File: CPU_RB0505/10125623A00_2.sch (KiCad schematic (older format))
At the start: 30 parts, among them IC1 TL16C750IPM, IC13 K9F1G08UOA-PCB0, IC14 74ACT16373, IC2 SN74ALVC164245, IC32 25LC320, IC38 74HCT1G08GW, IC39 74HCT04GW, IC5 74HCT1G32GW, IC7 29F400-70EC, IC8 SN74LVC1G07DBVT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

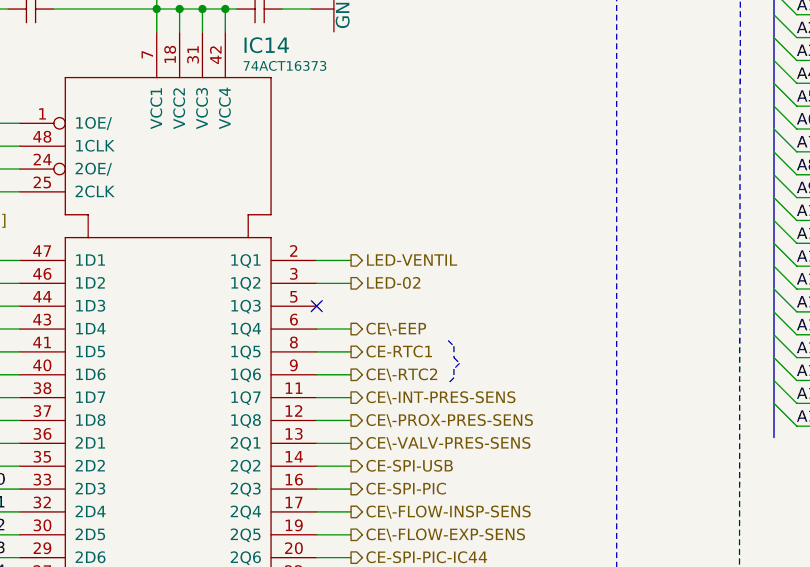
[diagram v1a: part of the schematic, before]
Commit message: Zero/Oh confusion: LED-02 => LED-O2, MRST-SPI-O_E => MRST-SPI-0_E
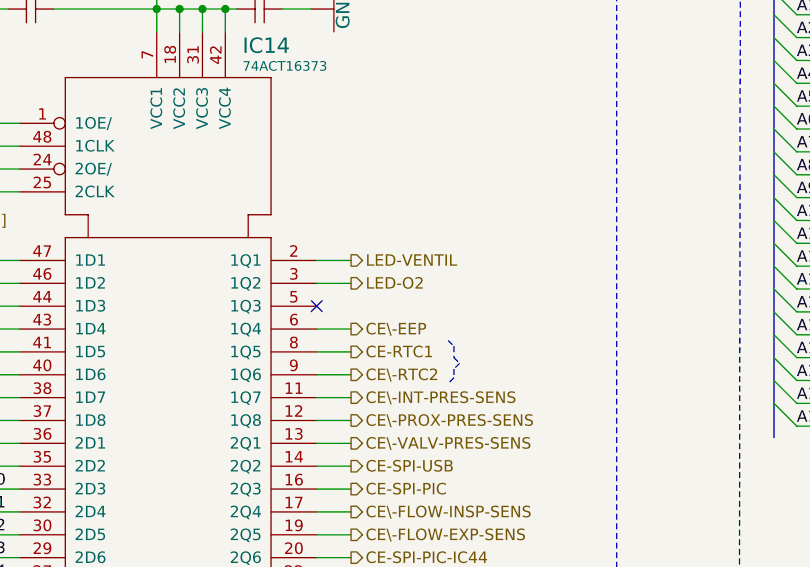
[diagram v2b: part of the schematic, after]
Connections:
- net LED-02 renamed LED-O2
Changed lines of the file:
@@
 LED-VENTIL
 Text HLabel 5625 2900 2    50   Output ~ 0
-LED-02
+LED-O2
 Text HLabel 5625 3100 2    50   Output ~ 0
 CE\-EEP

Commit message: back anotate from cmp file
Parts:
- C140, C15, C2, C24, C30, C33, C37, C4: footprint 10125623A00:C0805 -> AllModules:C0402_1
- C16: footprint 10125623A00:C0805 -> AllModules:C0603_1
- C20, C5: footprint 10125623A00:C0603 -> AllModules:C0402_1
- IC1: footprint 10125623A00:TQFP64 -> AllModules:TQFP64_1
- IC13, IC7: footprint 10125623A00:TS048 -> AllModules:TSOP48-ENT9.965_1
- IC14: footprint 10125623A00:TSSOP48 -> AllModules:SSOP48_1
- IC2: footprint 10125623A00:TSSOP48 -> AllModules:TSSOP48_1
- IC32: footprint 10125623A00:SOIC8 -> AllModules:MX.A8_COMPOSANT_1
- IC38, IC39, IC5: footprint 10125623A00:SOT23-5 -> AllModules:SC70-5_1
- IC8, IC9: footprint 10125623A00:SOT753_DBV -> AllModules:SOT23-5_1
- JP5, JP6: footprint 10125623A00:0805 -> AllModules:R0603_1
- Q2: footprint 10125623A00:HC49UP -> AllModules:HC49-4HSMX_1
- R2, R4, R5, R6: footprint 10125623A00:R0805 -> AllModules:R0603_1
- RS8: footprint 10125623A00:BCN16_4_ -> AllModules:BCN16_1
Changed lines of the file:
@@
 F 0 "C33" V 4450 1594 64  0000 L BNN
 F 1 "100nF" V 4356 1601 42  0000 L BNN
-F 2 "10125623A00:C0805" H 4225 1700 50  0001 C CNN
+F 2 "AllModules:C0402_1" H 4225 1700 50  0001 C CNN
 F 3 "" H 4225 1700 50  0001 C CNN
 F 4 "CAPACITOR,100NF,16V,+/-10%,X7R,0402" H 4225 1700 50  0001 C CNN "Description"
@@
 F 0 "C37" V 5450 1607 64  0000 L BNN
 F 1 "100nF" V 5356 1601 42  0000 L BNN
-F 2 "10125623A00:C0805" H 5225 1700 50  0001 C CNN
+F 2 "AllModules:C0402_1" H 5225 1700 50  0001 C CNN
 F 3 "" H 5225 1700 50  0001 C CNN
 F 4 "CAPACITOR,100NF,16V,+/-10%,X7R,0402" H 5225 1700 50  0001 C CNN "Description"
@@
 F 0 "C2" V 12487 1394 64  0000 R TNN
 F 1 "100nF" V 12418 1387 42  0000 R TNN
-F 2 "10125623A00:C0805" H 12325 1325 50  0001 C CNN
+F 2 "AllModules:C0402_1" H 12325 1325 50  0001 C CNN
 F 3 "" H 12325 1325 50  0001 C CNN
 F 4 "CAPACITOR,100NF,16V,+/-10%,X7R,0402" H 12325 1325 50  0001 C CNN "Description"
@@
 F 0 "Q2" V 13690 1950 64  0000 R TNN
 F 1 "3.6864MHz" V 13775 2188 42  0000 R TNN
-F 2 "10125623A00:HC49UP" H 13775 1750 50  0001 C CNN
+F 2 "AllModules:HC49-4HSMX_1" H 13775 1750 50  0001 C CNN
 F 3 "" H 13775 1750 50  0001 C CNN
 F 4 "CRYSTAL, QUARTZ, 3.6864MHZ" H 13775 1750 50  0001 C CNN "Description"
@@
 F 0 "C15" V 14162 2043 64  0000 R TNN
 F 1 "47pF" V 14256 2037 42  0000 R TNN
-F 2 "10125623A00:C0805" H 14075 1950 50  0001 C CNN
+F 2 "AllModules:C0402_1" H 14075 1950 50  0001 C CNN
 F 3 "" H 14075 1950 50  0001 C CNN
 F 4 "CAPACITOR,47 PF,+/-5%,50V,0402" H 14075 1950 50  0001 C CNN "Description"
@@
 F 0 "C16" V 14450 1432 64  0000 L BNN
 F 1 "22pF" V 14356 1438 42  0000 L BNN
-F 2 "10125623A00:C0805" H 14200 1525 50  0001 C CNN
+F 2 "AllModules:C0603_1" H 14200 1525 50  0001 C CNN
 F 3 "" H 14200 1525 50  0001 C CNN
 F 4 "CAPACITOR CERAMIC,22PF,+/-5%,50V,0603" H 14200 1525 50  0001 C CNN "Description"
@@
 F 0 "R2" H 13225 1800 64  0000 L BNN
 F 1 "1.5k" H 13225 1738 42  0000 L BNN
-F 2 "10125623A00:R0805" H 13300 1950 50  0001 C CNN
+F 2 "AllModules:R0603_1" H 13300 1950 50  0001 C CNN
 F 3 "" H 13300 1950 50  0001 C CNN
 F 4 "RESISTOR 1.5K OHM, 0603, +/-5%" H 13300 1950 50  0001 C CNN "Description"
@@
 F 0 "IC1" H 12650 4625 59  0000 L BNN
 F 1 "TL16C750IPM" H 12650 4538 42  0000 L BNN
-F 2 "10125623A00:TQFP64" H 12200 3000 50  0001 C CNN
+F 2 "AllModules:TQFP64_1" H 12200 3000 50  0001 C CNN
 F 3 "" H 12200 3000 50  0001 C CNN
 F 4 "UART, LQFP64" H 12200 3000 50  0001 C CNN "Description"
@@
 F 0 "RS8" V 13425 3425 59  0000 L BNN
 F 1 "6.8k" V 13338 3425 59  0000 L BNN
-F 2 "10125623A00:BCN16_4_" H 13350 3200 50  0001 C CNN
+F 2 "AllModules:BCN16_1" H 13350 3200 50  0001 C CNN
 F 3 "" H 13350 3200 50  0001 C CNN
 F 4 "RESISTOR ARRAY, 6.8K OHM, +/-5%, 1206" H 13350 3200 50  0001 C CNN "Description"
@@
 F 0 "IC8" H 14600 7112 64  0000 L BNN
 F 1 "SN74LVC1G07DBVT" H 14575 7025 42  0000 L BNN
-F 2 "10125623A00:SOT753_DBV" H 14250 6650 50  0001 C CNN
+F 2 "AllModules:SOT23-5_1" H 14250 6650 50  0001 C CNN
 F 3 "" H 14250 6650 50  0001 C CNN
 F 4 "BUFFER WITH OPEN DRAIN OUTPUT,SOT23" H 14250 6650 50  0001 C CNN "Description"
@@
 F 0 "R5" V 13613 3925 64  0000 R TNN
 F 1 "10k" V 13550 3925 42  0000 R TNN
-F 2 "10125623A00:R0805" H 13600 4000 50  0001 C CNN
+F 2 "AllModules:R0603_1" H 13600 4000 50  0001 C CNN
 F 3 "" H 13600 4000 50  0001 C CNN
 F 4 "RESISTOR,10K OHM, 0.063W,+/-5%,0603" H 13600 4000 50  0001 C CNN "Description"
@@
 F 0 "R6" V 15300 6200 64  0000 R TNN
 F 1 "10k" V 15225 6200 42  0000 R TNN
-F 2 "10125623A00:R0805" H 15275 6350 50  0001 C CNN
+F 2 "AllModules:R0603_1" H 15275 6350 50  0001 C CNN
 F 3 "" H 15275 6350 50  0001 C CNN
 F 4 "RESISTOR,10K OHM, 0.063W,+/-5%,0603" H 15275 6350 50  0001 C CNN "Description"
@@
 F 0 "C140" V 3000 1606 64  0000 L BNN
 F 1 "100nF" V 3069 1625 42  0000 L BNN
-F 2 "10125623A00:C0805" H 3150 1725 50  0001 C CNN
+F 2 "AllModules:C0402_1" H 3150 1725 50  0001 C CNN
 F 3 "" H 3150 1725 50  0001 C CNN
 	1    3150 1725
@@
 F 0 "C4" V 7125 6719 64  0000 L BNN
 F 1 "100nF" V 7031 6676 42  0000 L BNN
-F 2 "10125623A00:C0805" H 6900 6800 50  0001 C CNN
+F 2 "AllModules:C0402_1" H 6900 6800 50  0001 C CNN
 F 3 "" H 6900 6800 50  0001 C CNN
 F 4 "CAPACITOR,100NF,16V,+/-10%,X7R,0402" H 6900 6800 50  0001 C CNN "Description"
@@
 F 0 "C24" V 10887 6819 64  0000 R TNN
 F 1 "100nF" V 10818 6813 42  0000 R TNN
-F 2 "10125623A00:C0805" H 10725 6725 50  0001 C CNN
+F 2 "AllModules:C0402_1" H 10725 6725 50  0001 C CNN
 F 3 "" H 10725 6725 50  0001 C CNN
 F 4 "CAPACITOR,100NF,16V,+/-10%,X7R,0402" H 10725 6725 50  0001 C CNN "Description"
@@
 F 0 "C5" V 3825 6857 64  0000 L BNN
 F 1 "100nF" V 3731 6788 42  0000 L BNN
-F 2 "10125623A00:C0603" H 3600 6900 50  0001 C CNN
+F 2 "AllModules:C0402_1" H 3600 6900 50  0001 C CNN
 F 3 "" H 3600 6900 50  0001 C CNN
 F 4 "CAPACITOR,100NF,16V,+/-10%,X7R,0402" H 3600 6900 50  0001 C CNN "Description"
@@
 F 0 "C20" V 4800 6844 64  0000 L BNN
 F 1 "100nF" V 4706 6826 42  0000 L BNN
-F 2 "10125623A00:C0603" H 4575 6900 50  0001 C CNN
+F 2 "AllModules:C0402_1" H 4575 6900 50  0001 C CNN
 F 3 "" H 4575 6900 50  0001 C CNN
 F 4 "CAPACITOR,100NF,16V,+/-10%,X7R,0402" H 4575 6900 50  0001 C CNN "Description"
@@
 F 0 "JP6" H 14475 5525 51  0000 L BNN
 F 1 "JUMP_0U" H 14000 5525 51  0001 L BNN
-F 2 "10125623A00:0805" H 14550 5450 50  0001 C CNN
+F 2 "AllModules:R0603_1" H 14550 5450 50  0001 C CNN
 F 3 "" H 14550 5450 50  0001 C CNN
 F 4 "RESISTANCE, 0 OHM,0603" H 14550 5450 50  0001 C CNN "Description"
@@
 F 0 "IC13" H 7350 8625 64  0000 L BNN
 F 1 "K9F1G08UOA-PCB0" H 7350 8537 42  0000 L BNN
-F 2 "10125623A00:TS048" H 6400 7900 50  0001 C CNN
+F 2 "AllModules:TSOP48-ENT9.965_1" H 6400 7900 50  0001 C CNN
 F 3 "" H 6400 7900 50  0001 C CNN
 F 4 "MEMORY NAND FLASH, 1G, 2.7 TO 3.6V, BUS X 8,TSOP" H 6400 7900 50  0001 C CNN "Description"
@@
 F 0 "IC39" H 2238 2925 67  0000 L BNN
 F 1 "74HCT04GW" H 2238 2850 42  0000 L BNN
-F 2 "10125623A00:SOT23-5" H 1650 2175 50  0001 C CNN
+F 2 "AllModules:SC70-5_1" H 1650 2175 50  0001 C CNN
 F 3 "" H 1650 2175 50  0001 C CNN
 F 4 "IC, INVERTER,SOT353" H 1650 2175 50  0001 C CNN "Description"
@@
 F 0 "C30" V 8763 1356 64  0000 R TNN
 F 1 "100nF" V 8694 1350 42  0000 R TNN
-F 2 "10125623A00:C0805" H 8600 1300 50  0001 C CNN
+F 2 "AllModules:C0402_1" H 8600 1300 50  0001 C CNN
 F 3 "" H 8600 1300 50  0001 C CNN
 F 4 "CAPACITOR,100NF,16V,+/-10%,X7R,0402" H 8600 1300 50  0001 C CNN "Description"
@@
 F 0 "IC7" H 8975 4725 64  0000 L BNN
 F 1 "29F400-70EC" H 8975 4650 42  0000 L BNN
-F 2 "10125623A00:TS048" H 8575 3125 50  0001 C CNN
+F 2 "AllModules:TSOP48-ENT9.965_1" H 8575 3125 50  0001 C CNN
 F 3 "" H 8575 3125 50  0001 C CNN
 F 4 "IC, FLASH MEMORY,TSOP48" H 8575 3125 50  0001 C CNN "Description"
@@
 F 0 "IC38" H 3350 3425 67  0000 L BNN
 F 1 "74HCT1G08GW" H 3337 3350 42  0000 L BNN
-F 2 "10125623A00:SOT23-5" H 2800 2675 50  0001 C CNN
+F 2 "AllModules:SC70-5_1" H 2800 2675 50  0001 C CNN
 F 3 "" H 2800 2675 50  0001 C CNN
 F 4 "2 INPUT AND-GATE,SOT353" H 2800 2675 50  0001 C CNN "Description"
@@
 F 0 "IC14" H 5150 4900 67  0000 L BNN
 F 1 "74ACT16373" H 5150 4825 42  0000 L BNN
-F 2 "10125623A00:TSSOP48" H 4875 3400 50  0001 C CNN
+F 2 "AllModules:SSOP48_1" H 4875 3400 50  0001 C CNN
 F 3 "" H 4875 3400 50  0001 C CNN
 F 4 "IC,16 BIT D TYPE 3STATE OP, LATCHES,SSOP" H 4875 3400 50  0001 C CNN "Description"
@@
 F 0 "IC9" H 14275 3775 64  0000 L BNN
 F 1 "SN74LVC1G07DBVT" H 13825 3875 42  0000 L BNN
-F 2 "10125623A00:SOT753_DBV" H 14400 4250 50  0001 C CNN
+F 2 "AllModules:SOT23-5_1" H 14400 4250 50  0001 C CNN
 F 3 "" H 14400 4250 50  0001 C CNN
 F 4 "BUFFER WITH OPEN DRAIN OUTPUT,SOT23" H 14400 4250 50  0001 C CNN "Description"
@@
 F 0 "JP5" H 14225 5525 51  0000 L BNN
 F 1 "JUMP_0U" H 13875 5800 51  0001 L BNN
-F 2 "10125623A00:0805" H 14300 5450 50  0001 C CNN
+F 2 "AllModules:R0603_1" H 14300 5450 50  0001 C CNN
 F 3 "" H 14300 5450 50  0001 C CNN
 	1    14300 5450
@@
 F 0 "R4" V 13625 1838 64  0000 L BNN
 F 1 "1M" V 13538 1875 42  0000 L BNN
-F 2 "10125623A00:R0805" H 13550 1750 50  0001 C CNN
+F 2 "AllModules:R0603_1" H 13550 1750 50  0001 C CNN
 F 3 "" H 13550 1750 50  0001 C CNN
 F 4 "RESISTOR,1M OHM,0.063W,+/-1%,0603" H 13550 1750 50  0001 C CNN "Description"
@@
 F 0 "IC2" H 5100 8275 67  0000 R TNN
 F 1 "SN74ALVC164245" H 5500 8175 42  0000 R TNN
-F 2 "10125623A00:TSSOP48" H 3225 7700 50  0001 C CNN
+F 2 "AllModules:TSSOP48_1" H 3225 7700 50  0001 C CNN
 F 3 "" H 3225 7700 50  0001 C CNN
 F 4 "TRANSCEIVER, 3.3V TO 5V,TSSOP" H 3225 7700 50  0001 C CNN "Description"
@@
 F 0 "IC5" H 2250 9113 64  0000 L BNN
 F 1 "74HCT1G32GW" H 2250 9038 42  0000 L BNN
-F 2 "10125623A00:SOT23-5" H 1700 8350 50  0001 C CNN
+F 2 "AllModules:SC70-5_1" H 1700 8350 50  0001 C CNN
 F 3 "" H 1700 8350 50  0001 C CNN
 F 4 "IC, 2 INPUT OR-GATE,SOT353" H 1700 8350 50  0001 C CNN "Description"
@@
 F 0 "IC32" H 10987 8287 67  0000 L BNN
 F 1 "25LC320" H 10987 8212 42  0000 L BNN
-F 2 "10125623A00:SOIC8" H 10325 7575 50  0001 C CNN
+F 2 "AllModules:MX.A8_COMPOSANT_1" H 10325 7575 50  0001 C CNN
 F 3 "" H 10325 7575 50  0001 C CNN
 F 4 "EEPROM, SOIC8" H 10325 7575 50  0001 C CNN "Description"

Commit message: fix erc errors, change many pin electrical types
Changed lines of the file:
@@
 $Descr User 17335 11946
 encoding utf-8
-Sheet 6 8
+Sheet 5 8
 Title "RB0505 CPU Board"
 Date "2020-04-15"
@@
 Wire Bus Line
 	7475 1525 7475 3575
+$Comp
+L power:PWR_FLAG #FLG0109
+U 1 1 6003889E
+P 14100 5650
+F 0 "#FLG0109" H 14100 5725 50  0001 C CNN
+F 1 "PWR_FLAG" V 14100 5777 50  0000 L CNN
+F 2 "" H 14100 5650 50  0001 C CNN
+F 3 "~" H 14100 5650 50  0001 C CNN
+	1    14100 5650
+	0    -1   -1   0
+$EndComp
+Connection ~ 14100 5650
 $EndSCHEMATC

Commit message: CPU schematic updated to Kicad resistor and cap symbols
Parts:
- C140, C15, C16, C2, C24, C30, C33, C37, C4: symbol cpu-board:C0805 -> Flipped_Devices:C_Small
- C20, C5: symbol cpu-board:C0603 -> Flipped_Devices:C_Small
- R2, R4, R5, R6: symbol cpu-board:R0805 -> Flipped_Devices:R
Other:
- moved on the sheet: C140, C16, C2, C20, C24, C30, C33, C37, C5, IC14, IC2, IC32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

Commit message: CPU board diode and transistor symbols changed to Kicad symbols
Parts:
- Q2: symbol cpu-board:HC49UP -> Device:Crystal_Small
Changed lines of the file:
@@
 $EndComp
 $Comp
-L cpu-board:HC49UP Q2
+L Device:Crystal_Small Q2
 U 1 1 53ABB1EB
 P 13800 1750

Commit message: ran renameSchSyms.py
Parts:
- C140, C2, C20, C24, C30, C33, C37, C4, C5: symbol Flipped_Devices:C_Small -> Capacitor:C0402_100nF_16V_10%
- C15: symbol Flipped_Devices:C_Small -> Capacitor:C0402_47pF_50V_5%
- C16: symbol Flipped_Devices:C_Small -> Capacitor:C0603_22pF_50V_5%
- IC1: symbol cpu-board:TL16C750IPM -> IC:TL16C750IPM
- IC13: symbol cpu-board:K9F4G08U0M-PCB000 -> IC:K9F4G08U0M-PCB000
- IC14: symbol cpu-board:74ACT16373 -> IC:74ACT16373
- IC2: symbol cpu-board:SN74ALVC164245 -> IC:SN74ALVC164245
- IC32: symbol cpu-board:AT25--- -> IC:AT25---
- IC38: symbol cpu-board:74HCT1G08GW -> IC:74HCT1G08GW
- IC39: symbol cpu-board:74HCT1G04GW -> IC:74HCT1G04GW
- IC5: symbol cpu-board:74HCT1G32GW -> IC:74HCT1G32GW
- IC7: symbol cpu-board:29F800 -> IC:29F800
- IC8, IC9: symbol cpu-board:LVC1G07DBVT -> IC:LVC1G07DBVT
- JP6: symbol cpu-board:JUMP_0U -> Jumper:JUMP_0U
- Q2: symbol Device:Crystal_Small -> Crystal:Crystal_Small_10023291
- R2: symbol Flipped_Devices:R -> Resistor:R0603_1k5_5%
- R4: symbol Flipped_Devices:R -> Resistor:R0603_1M_1%
- R5, R6: symbol Flipped_Devices:R -> Resistor:R0603_10k_5%
- RS8: symbol cpu-board:RES_4R_BCN -> Resistor:R1206_6k8_5%
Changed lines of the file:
@@
 $EndComp
 $Comp
-L Flipped_Devices:C_Small C33
+L Capacitor:C0402_100nF_16V_10% C33
 U 1 1 C9502F30
 P 4250 1700
@@
 $EndComp
 $Comp
-L Flipped_Devices:C_Small C37
+L Capacitor:C0402_100nF_16V_10% C37
 U 1 1 235E1F38
 P 5250 1700
@@
 $EndComp
 $Comp
-L Flipped_Devices:C_Small C2
+L Capacitor:C0402_100nF_16V_10% C2
 U 1 1 6D294609
 P 12300 1300
@@
 $EndComp
 $Comp
-L Device:Crystal_Small Q2
+L Crystal:Crystal_Small_10023291 Q2
 U 1 1 53ABB1EB
 P 13800 1750
@@
 $EndComp
 $Comp
-L Flipped_Devices:C_Small C15
+L Capacitor:C0402_47pF_50V_5% C15
 U 1 1 58269073
 P 14075 1950
@@
 $EndComp
 $Comp
-L Flipped_Devices:R R2
+L Resistor:R0603_1k5_5% R2
 U 1 1 986554BD
 P 13300 1950
@@
 $EndComp
 $Comp
-L cpu-board:TL16C750IPM IC1
+L IC:TL16C750IPM IC1
 U 1 1 22F7723E
 P 12200 3000
@@
 $EndComp
 $Comp
-L cpu-board:RES_4R_BCN RS8
+L Resistor:R1206_6k8_5% RS8
 U 1 1 887C726F
 P 13350 3200
@@
 $EndComp
 $Comp
-L cpu-board:LVC1G07DBVT IC8
+L IC:LVC1G07DBVT IC8
 U 1 1 45D38355
 P 14250 6650
@@
 $EndComp
 $Comp
-L Flipped_Devices:R R5
+L Resistor:R0603_10k_5% R5
 U 1 1 40871C63
 P 13600 4000
@@
 $EndComp
 $Comp
-L Flipped_Devices:R R6
+L Resistor:R0603_10k_5% R6
 U 1 1 91847459
 P 15250 6350
@@
 $EndComp
 $Comp
-L Flipped_Devices:C_Small C140
+L Capacitor:C0402_100nF_16V_10% C140
 U 1 1 63F00A8C
 P 3150 1750
@@
 $EndComp
 $Comp
-L Flipped_Devices:C_Small C4
+L Capacitor:C0402_100nF_16V_10% C4
 U 1 1 A60240AA
 P 6900 6800
@@
 $EndComp
 $Comp
-L Flipped_Devices:C_Small C5
+L Capacitor:C0402_100nF_16V_10% C5
 U 1 1 8E04CE4C
 P 3575 6900
@@
 $EndComp
 $Comp
-L Flipped_Devices:C_Small C20
+L Capacitor:C0402_100nF_16V_10% C20
 U 1 1 D1510C23
 P 4550 6900
@@
 $EndComp
 $Comp
-L cpu-board:JUMP_0U JP6
+L Jumper:JUMP_0U JP6
 U 1 1 A21E5090
 P 14550 5450
@@
 $EndComp
 $Comp
-L cpu-board:K9F4G08U0M-PCB000 IC13
+L IC:K9F4G08U0M-PCB000 IC13
 U 1 1 B5257A37
 P 6400 7900
@@
 $EndComp
 $Comp
-L cpu-board:74HCT1G04GW IC39
+L IC:74HCT1G04GW IC39
 U 1 1 6BD6C1A1
 P 1650 2200
@@
 $EndComp
 $Comp
-L Flipped_Devices:C_Small C30
+L Capacitor:C0402_100nF_16V_10% C30
 U 1 1 107458DA
 P 8575 1300
@@
 $EndComp
 $Comp
-L cpu-board:29F800 IC7
+L IC:29F800 IC7
 U 1 1 270F9871
 P 8550 3100
@@
 	1600 2550 2700 2550
 $Comp
-L cpu-board:74HCT1G08GW IC38
+L IC:74HCT1G08GW IC38
 U 1 1 E1DA1C65
 P 2800 2700
@@
 	3600 2400 3750 2400
 $Comp
-L cpu-board:74ACT16373 IC14
+L IC:74ACT16373 IC14
 U 1 1 6BA2D255
 P 4850 3400
@@
 	8950 4400 8950 4550
 $Comp
-L cpu-board:LVC1G07DBVT IC9
+L IC:LVC1G07DBVT IC9
 U 1 1 5F7D4A82
 P 14400 4250
@@
 Connection ~ 13200 2775
 $Comp
-L Flipped_Devices:R R4
+L Resistor:R0603_1M_1% R4
 U 1 1 BADBB996
 P 13550 1750
@@
 CS0\
 $Comp
-L cpu-board:SN74ALVC164245 IC2
+L IC:SN74ALVC164245 IC2
 U 1 1 BC34DC86
 P 3200 7700
@@
 WR\
 $Comp
-L cpu-board:74HCT1G32GW IC5
+L IC:74HCT1G32GW IC5
 U 1 1 E8297B24
 P 1700 8350
@@
 D[0..15]
 $Comp
-L cpu-board:AT25--- IC32
+L IC:AT25--- IC32
 U 1 1 1703D4A9
 P 10350 7550
@@
 $EndComp
 $Comp
-L Flipped_Devices:C_Small C16
+L Capacitor:C0603_22pF_50V_5% C16
 U 1 1 8F520983
 P 14200 1500
@@
 	15250 6650 15450 6650
 $Comp
-L Flipped_Devices:C_Small C24
+L Capacitor:C0402_100nF_16V_10% C24
 U 1 1 7752927D
 P 10750 6700
